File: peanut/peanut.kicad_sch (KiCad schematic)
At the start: 39 parts, among them J1 USB-C, Q1 NMOS, U1 MS5611-01BA, U3 ESP32-C3FH4, Y1 40MHz

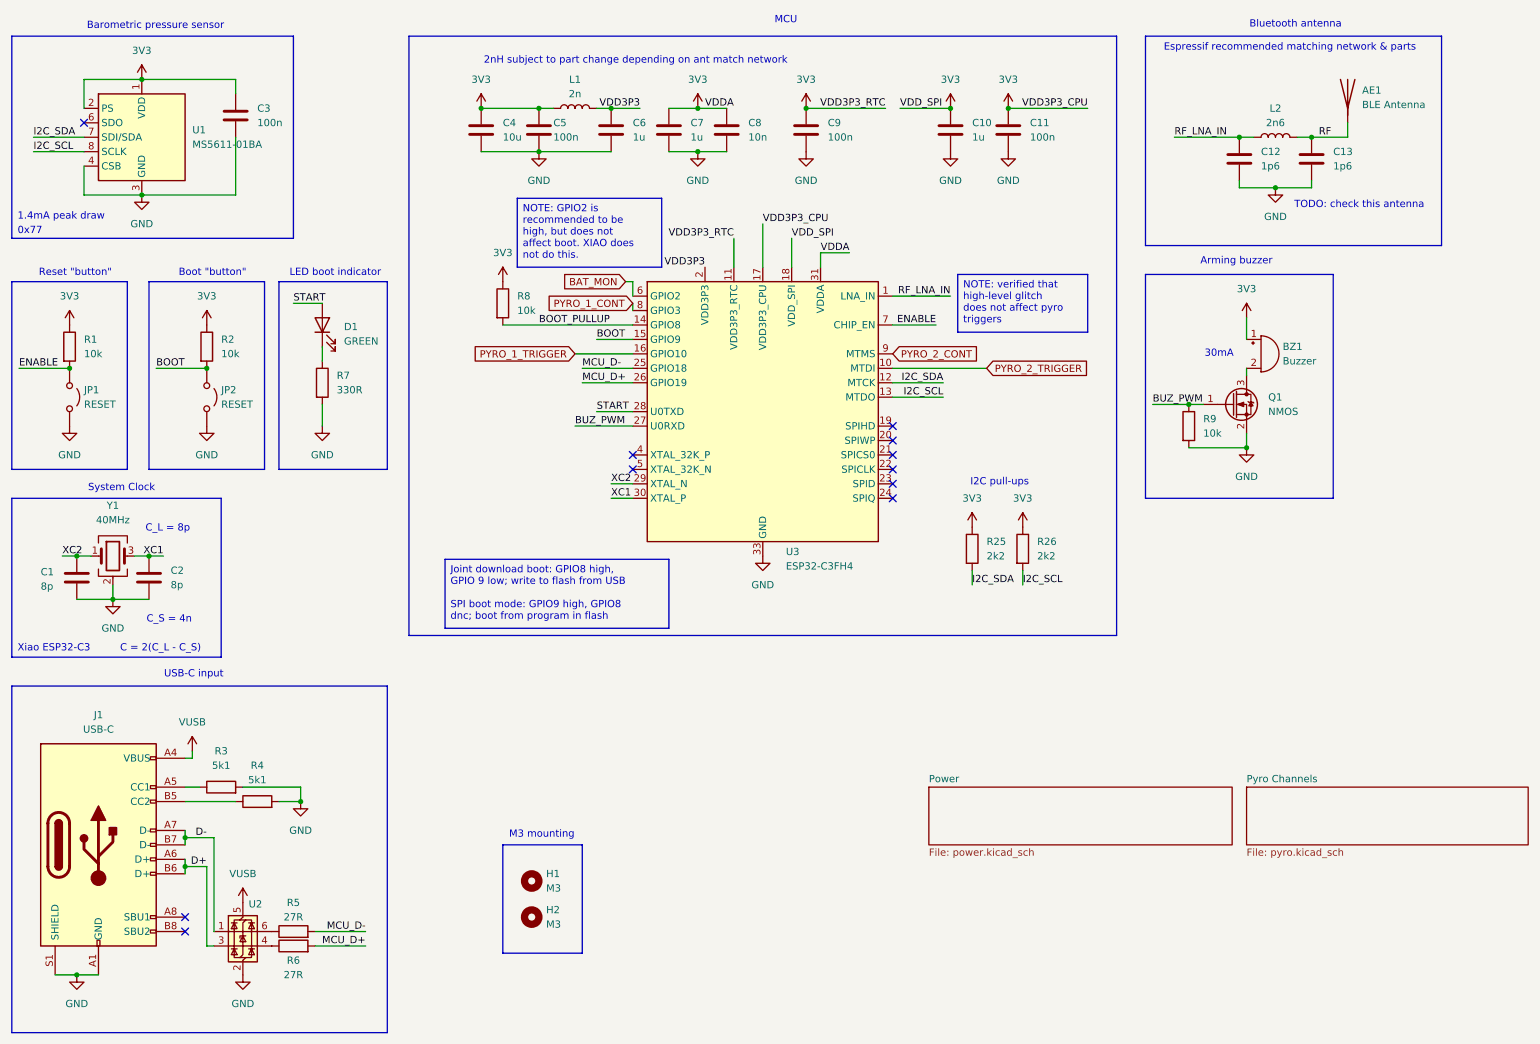
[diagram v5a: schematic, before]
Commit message: feat: Verify component features
Completed most of the review checklist for the initial revision. Routing
can commence once design rules are updated.
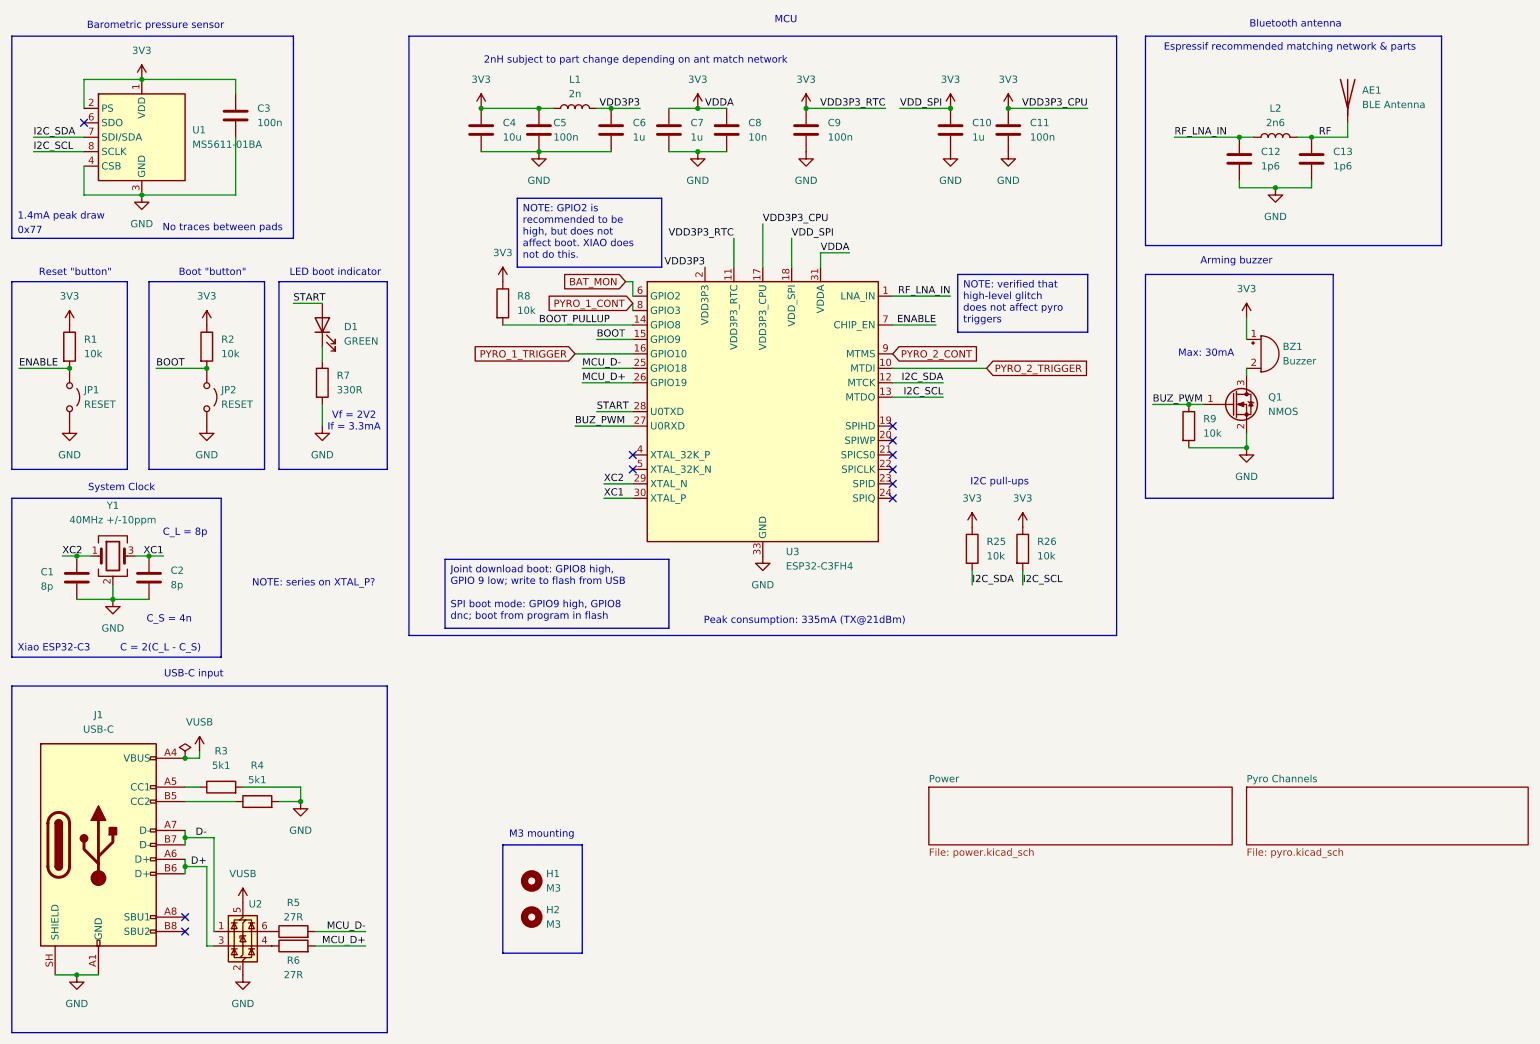
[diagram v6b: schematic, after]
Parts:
- R25, R26: value 2k2 -> 10k; MPN ERA-2AEB222X -> SFR01MZPJ103
- Y1: value 40MHz -> 40MHz +/-10ppm
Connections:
- net GND: now also J1.SH (SHIELD); no longer J1.S1 (SHIELD)
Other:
- note added: "Max: 30mA"
- note added: "NOTE: series on XTAL_P?"
- note added: "No traces between pads"
- note added: "Peak consumption: 335mA (TX@21dBm)"
- note added: "Vf = 2V2 If = 3.3mA"
- note removed: "30mA"
- note removed: "TODO: check this antenna"
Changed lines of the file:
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@@
 		)
 	)
+	(text "Peak consumption: 335mA (TX@21dBm)"
+		(exclude_from_sim no)
+		(at 154.686 123.19 0)
+		(effects
+			(font
+				(size 1.27 1.27)
+			)
+		)
+	)
 	(text "I2C pull-ups"
 		(exclude_from_sim no)
@@
 		)
 	)
-	(text "TODO: check this antenna"
+	(text "Max: 30mA"
 		(exclude_from_sim no)
-		(at 240.792 50.038 0)
+		(at 225.298 76.2 0)
 		(effects
 			(font
 				(size 1.27 1.27)
 			)
-			(justify left)
 		)
 	)
-	(text "30mA"
+	(text "Xiao ESP32-C3"
 		(exclude_from_sim no)
-		(at 227.584 76.2 0)
+		(at 16.256 128.016 0)
 		(effects
 			(font
 				(size 1.27 1.27)
 			)
+			(justify left)
 		)
 	)
-	(text "Xiao ESP32-C3"
+	(text "No traces between pads"
 		(exclude_from_sim no)
-		(at 16.256 128.016 0)
+		(at 52.324 54.102 0)
 		(effects
 			(font
 				(size 1.27 1.27)
 			)
-			(justify left)
 		)
 	)
@@
 		)
 	)
+	(text "NOTE: series on XTAL_P?"
+		(exclude_from_sim no)
+		(at 68.326 116.586 0)
+		(effects
+			(font
+				(size 1.27 1.27)
+			)
+		)
+	)
 	(text "LED boot indicator"
 		(exclude_from_sim no)
@@
 		)
 	)
+	(text "Vf = 2V2\nIf = 3.3mA"
+		(exclude_from_sim no)
+		(at 75.438 88.138 0)
+		(effects
+			(font
+				(size 1.27 1.27)
+			)
+		)
+	)
 	(text "MCU"
 		(exclude_from_sim no)
@@
 	(text "C_L = 8p"
 		(exclude_from_sim no)
-		(at 42.672 106.934 0)
+		(at 45.72 107.696 0)
 		(effects
 			(font
@@
 	)
 	(junction
+		(at 45.72 147.32)
+		(diameter 0)
+		(color 0 0 0 0)
+	)
+	(junction
 		(at 237.49 46.99)
 		(diameter 0)
@@
 	(wire
 		(pts
-			(xy 120.65 99.06) (xy 124.46 99.06)
+			(xy 119.38 99.06) (xy 124.46 99.06)
+		)
+		(stroke
+			(width 0)
+			(type default)
+		)
+	)
+	(wire
+		(pts
+			(xy 45.72 147.32) (xy 48.26 147.32)
 		)
 		(stroke
@@
 	(wire
 		(pts
-			(xy 46.99 147.32) (xy 45.72 147.32)
-		)
-		(stroke
-			(width 0)
-			(type default)
-		)
-	)
-	(wire
-		(pts
 			(xy 26.67 185.42) (xy 30.48 185.42)
 		)
@@
 	(wire
 		(pts
-			(xy 46.99 146.05) (xy 46.99 147.32)
+			(xy 48.26 146.05) (xy 48.26 147.32)
 		)
 		(stroke
@@
 	(wire
 		(pts
-			(xy 120.65 101.6) (xy 124.46 101.6)
+			(xy 119.38 101.6) (xy 124.46 101.6)
 		)
 		(stroke
@@
 	)
 	(label "XC2"
-		(at 120.65 99.06 0)
+		(at 119.38 99.06 0)
 		(effects
 			(font
@@
 	)
 	(label "XC1"
-		(at 120.65 101.6 0)
+		(at 119.38 101.6 0)
 		(effects
 			(font
@@
 			)
 		)
-		(property "Value" "40MHz"
+		(property "Value" "40MHz +/-10ppm"
 			(at 33.02 105.41 0)
 			(show_name no)
@@
 	(symbol
 		(lib_id "power:VBUS")
-		(at 46.99 146.05 0)
+		(at 48.26 146.05 0)
 		(unit 1)
 		(body_style 1)
@@
 		(fields_autoplaced yes)
 		(property "Reference" "#PWR07"
-			(at 46.99 149.86 0)
+			(at 48.26 149.86 0)
 			(hide yes)
 			(show_name no)
@@
 		)
 		(property "Value" "VUSB"
-			(at 46.99 140.97 0)
+			(at 48.26 140.97 0)
 			(show_name no)
 			(do_not_autoplace no)
@@
 		)
 		(property "Footprint" ""
-			(at 46.99 146.05 0)
+			(at 48.26 146.05 0)
 			(hide yes)
 			(show_name no)
@@
 		)
 		(property "Datasheet" ""
-			(at 46.99 146.05 0)
+			(at 48.26 146.05 0)
 			(hide yes)
 			(show_name no)
@@
 		)
 		(property "Description" "Power symbol creates a global label with name \"VBUS\""
-			(at 46.99 146.05 0)
+			(at 48.26 146.05 0)
 			(hide yes)
 			(show_name no)
@@
 			)
 		)
-		(property "Value" "2k2"
+		(property "Value" "10k"
 			(at 186.69 111.7599 0)
 			(show_name no)
@@
 			)
 		)
-		(property "Datasheet" "https://industrial.panasonic.com/cdbs/www-data/pdf/RDM0000/AOA0000C307.pdf"
+		(property "Datasheet" ""
 			(at 184.15 110.49 0)
 			(hide yes)
@@
 			)
 		)
-		(property "MPN" "ERA-2AEB222X"
+		(property "MPN" "SFR01MZPJ103"
 			(at 184.15 110.49 0)
 			(hide yes)
@@
 		(pin "A1"
 		)
-		(pin "S1"
+		(pin "SH"
 		)
 		(pin "A4"
@@
 	)
 	(symbol
+		(lib_id "power:PWR_FLAG")
+		(at 45.72 147.32 0)
+		(unit 1)
+		(body_style 1)
+		(exclude_from_sim no)
+		(in_bom yes)
+		(on_board yes)
+		(in_pos_files yes)
+		(dnp no)
+		(fields_autoplaced yes)
+		(property "Reference" "#FLG04"
+			(at 45.72 145.415 0)
+			(hide yes)
+			(show_name no)
+			(do_not_autoplace no)
+			(effects
+				(font
+					(size 1.27 1.27)
+				)
+			)
+		)
+		(property "Value" ""
+			(at 45.72 142.24 0)
+			(show_name no)
+			(do_not_autoplace no)
+			(effects
+				(font
+					(size 1.27 1.27)
+				)
+			)
+		)
+		(property "Footprint" ""
+			(at 45.72 147.32 0)
+			(hide yes)
+			(show_name no)
+			(do_not_autoplace no)
+			(effects
+				(font
+					(size 1.27 1.27)
+				)
+			)
+		)
+		(property "Datasheet" ""
+			(at 45.72 147.32 0)
+			(hide yes)
+			(show_name no)
+			(do_not_autoplace no)
+			(effects
+				(font
+					(size 1.27 1.27)
+				)
+			)
+		)
+		(property "Description" "Special symbol for telling ERC where power comes from"
+			(at 45.72 147.32 0)
+			(hide yes)
+			(show_name no)
+			(do_not_autoplace no)
+			(effects
+				(font
+					(size 1.27 1.27)
+				)
+			)
+		)
+		(pin "1"
+		)
+		(instances
+			(project "peanut"
+				(path "/5c6b6cfc-6c84-425a-9b66-e6111713aae8"
+					(reference "#FLG04")
+					(unit 1)
+				)
+			)
+		)
+	)
+	(symbol
 		(lib_id "Mechanical:MountingHole")
 		(at 106.68 168.91 0)
@@
 			)
 		)
-		(property "Value" "2k2"
+		(property "Value" "10k"
 			(at 195.58 111.7599 0)
 			(show_name no)
@@
 			)
 		)
-		(property "Datasheet" "https://industrial.panasonic.com/cdbs/www-data/pdf/RDM0000/AOA0000C307.pdf"
+		(property "Datasheet" ""
 			(at 193.04 110.49 0)
 			(hide yes)
@@
 			)
 		)
-		(property "MPN" "ERA-2AEB222X"
+		(property "MPN" "SFR01MZPJ103"
 			(at 193.04 110.49 0)
 			(hide yes)

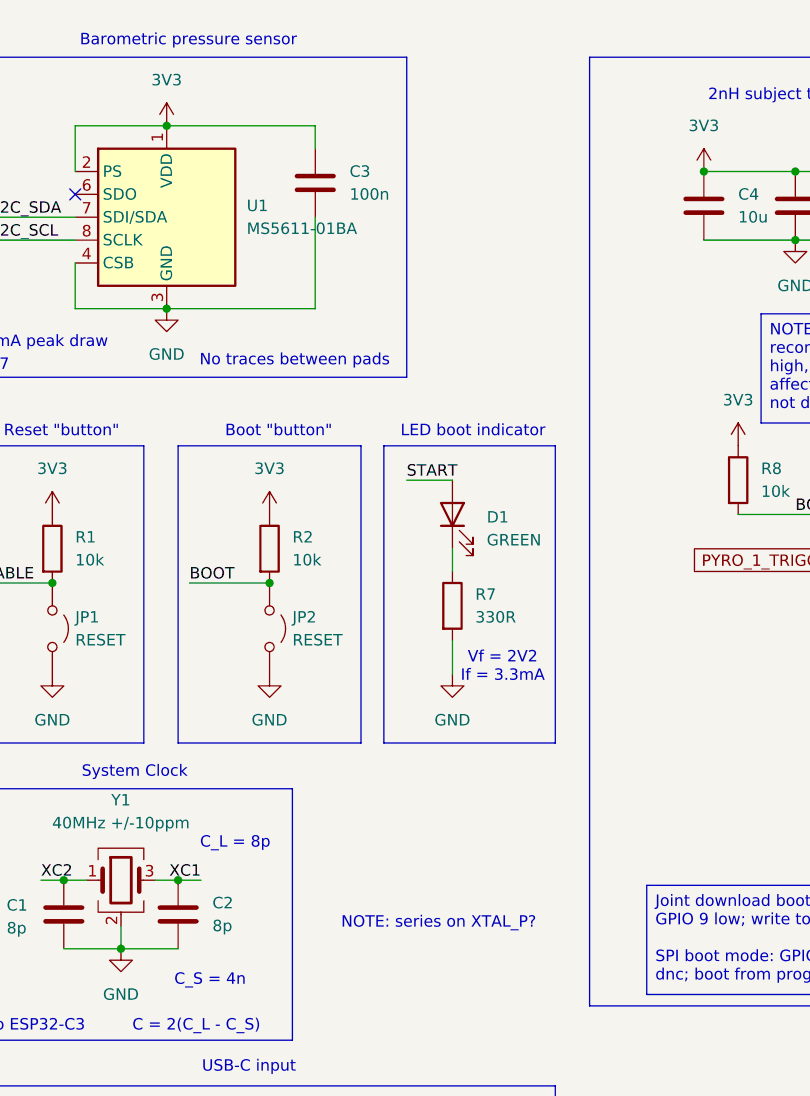
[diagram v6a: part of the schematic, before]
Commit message: feat: Cheaper inductor
Swapped inductor for one that is cheaper. Current board cost (minus JST
connector since that is not available on Mouser) is $44.76 CAD in
components.
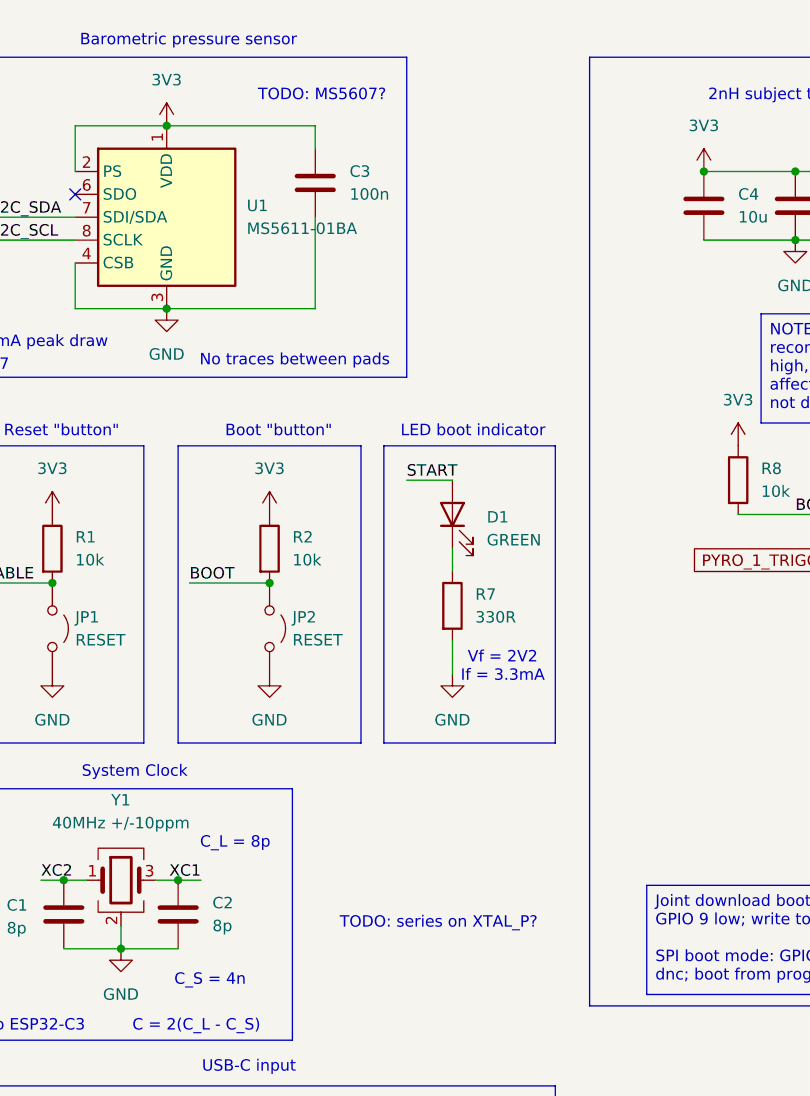
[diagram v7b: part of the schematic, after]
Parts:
- JP1, JP2: MPN - -> (none)
- R1, R2, R25, R26, R8, R9: MPN SFR01MZPJ103 -> MCS04020C1002FE000
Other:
- note added: "TODO: MS5607?"
- note added: "TODO: series on XTAL_P?"
- note removed: "NOTE: series on XTAL_P?"
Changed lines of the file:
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@@
 		)
 	)
-	(text "NOTE: series on XTAL_P?"
+	(text "TODO: MS5607?"
+		(exclude_from_sim no)
+		(at 55.372 24.638 0)
+		(effects
+			(font
+				(size 1.27 1.27)
+			)
+		)
+	)
+	(text "TODO: series on XTAL_P?"
 		(exclude_from_sim no)
 		(at 68.326 116.586 0)
@@
 			)
 		)
-		(property "MPN" "SFR01MZPJ103"
+		(property "MPN" "MCS04020C1002FE000"
 			(at 184.15 110.49 0)
 			(hide yes)
@@
 			)
 		)
-		(property "MPN" "SFR01MZPJ103"
+		(property "MPN" "MCS04020C1002FE000"
 			(at 25.4 74.93 0)
 			(hide yes)
@@
 			)
 		)
-		(property "MPN" "SFR01MZPJ103"
+		(property "MPN" "MCS04020C1002FE000"
 			(at 101.6 67.31 0)
 			(hide yes)
@@
 			)
 		)
-		(property "MPN" "-"
+		(property "MPN" ""
 			(at 49.53 83.82 90)
 			(hide yes)
@@
 			)
 		)
-		(property "MPN" "SFR01MZPJ103"
+		(property "MPN" "MCS04020C1002FE000"
 			(at 49.53 74.93 0)
 			(hide yes)
@@
 			)
 		)
-		(property "MPN" "-"
+		(property "MPN" ""
 			(at 25.4 83.82 90)
 			(hide yes)
@@
 			)
 		)
-		(property "MPN" "SFR01MZPJ103"
+		(property "MPN" "MCS04020C1002FE000"
 			(at 193.04 110.49 0)
 			(hide yes)
@@
 			)
 		)
-		(property "MPN" "SFR01MZPJ103"
+		(property "MPN" "MCS04020C1002FE000"
 			(at 222.25 88.9 0)
 			(hide yes)

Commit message: feat: Solder jumpers instead of capacitor footprint
The boot and enable jumpers are now solder jumpers instead of capacitors
footprints, which should make them easier to jump.
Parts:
- JP1, JP2: footprint Capacitor_SMD:C_0805_2012Metric -> Jumper:SolderJumper-2_P1.3mm_Open_TrianglePad1.0x1.5mm
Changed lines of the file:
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@@
 			)
 		)
-		(property "Footprint" "Capacitor_SMD:C_0805_2012Metric"
+		(property "Footprint" "Jumper:SolderJumper-2_P1.3mm_Open_TrianglePad1.0x1.5mm"
 			(at 49.53 83.82 0)
 			(hide yes)
@@
 			)
 		)
-		(property "Footprint" "Capacitor_SMD:C_0805_2012Metric"
+		(property "Footprint" "Jumper:SolderJumper-2_P1.3mm_Open_TrianglePad1.0x1.5mm"
 			(at 25.4 83.82 0)
 			(hide yes)
